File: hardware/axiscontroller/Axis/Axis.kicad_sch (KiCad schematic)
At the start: 62 parts, among them J1 RS485, J10 Fan, J2 Motor, J3 Limits, J4 RS485, J5 Console, J6 Temp A, J7 Temp B, J8 Brake, J9 Power, Q1 Q_NMOS, Q2 Q_NMOS, SW1 SW_DIP_x04, U4 TLP291, U5 TLP291, U6 TLP291, U7 MAX485CPA, U8 74AHCT125

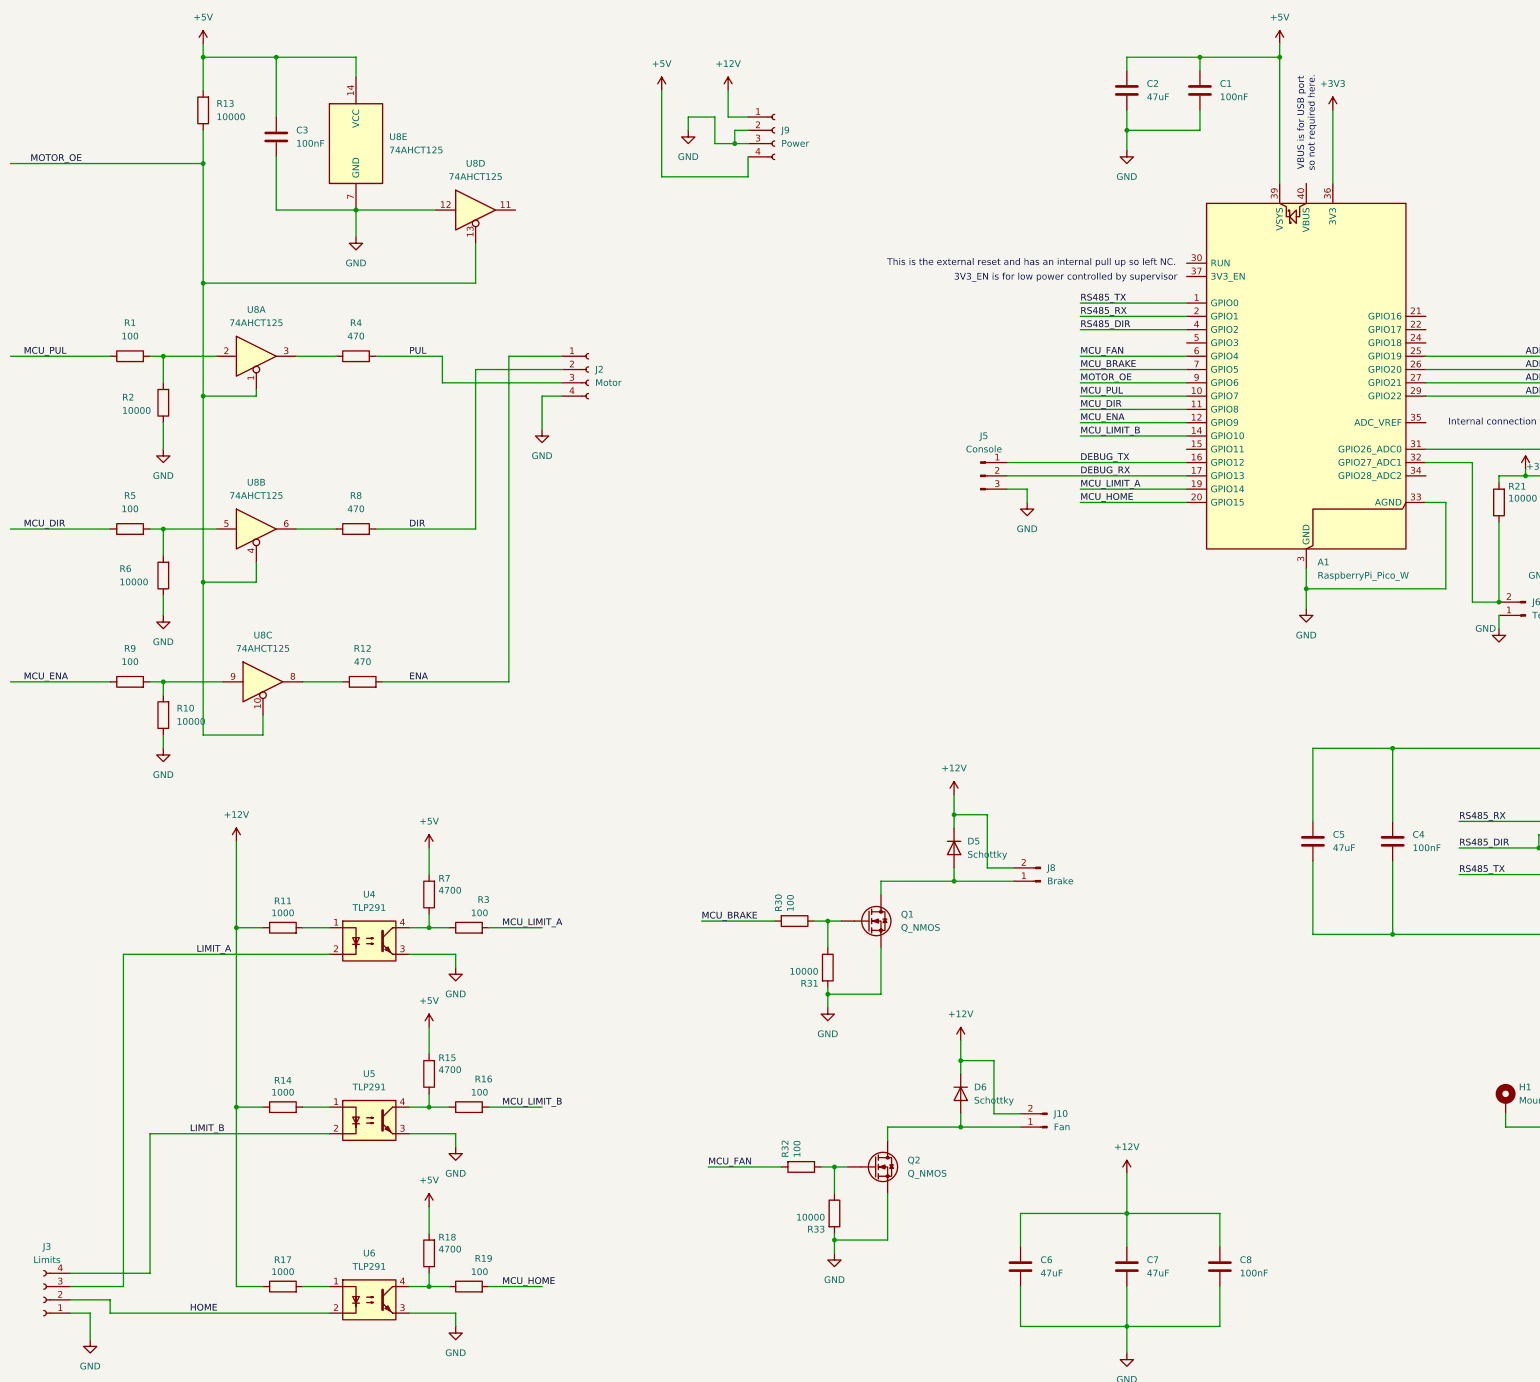
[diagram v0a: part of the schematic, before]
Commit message: Fix ERC warnings/errors and add IRLR8726 component.
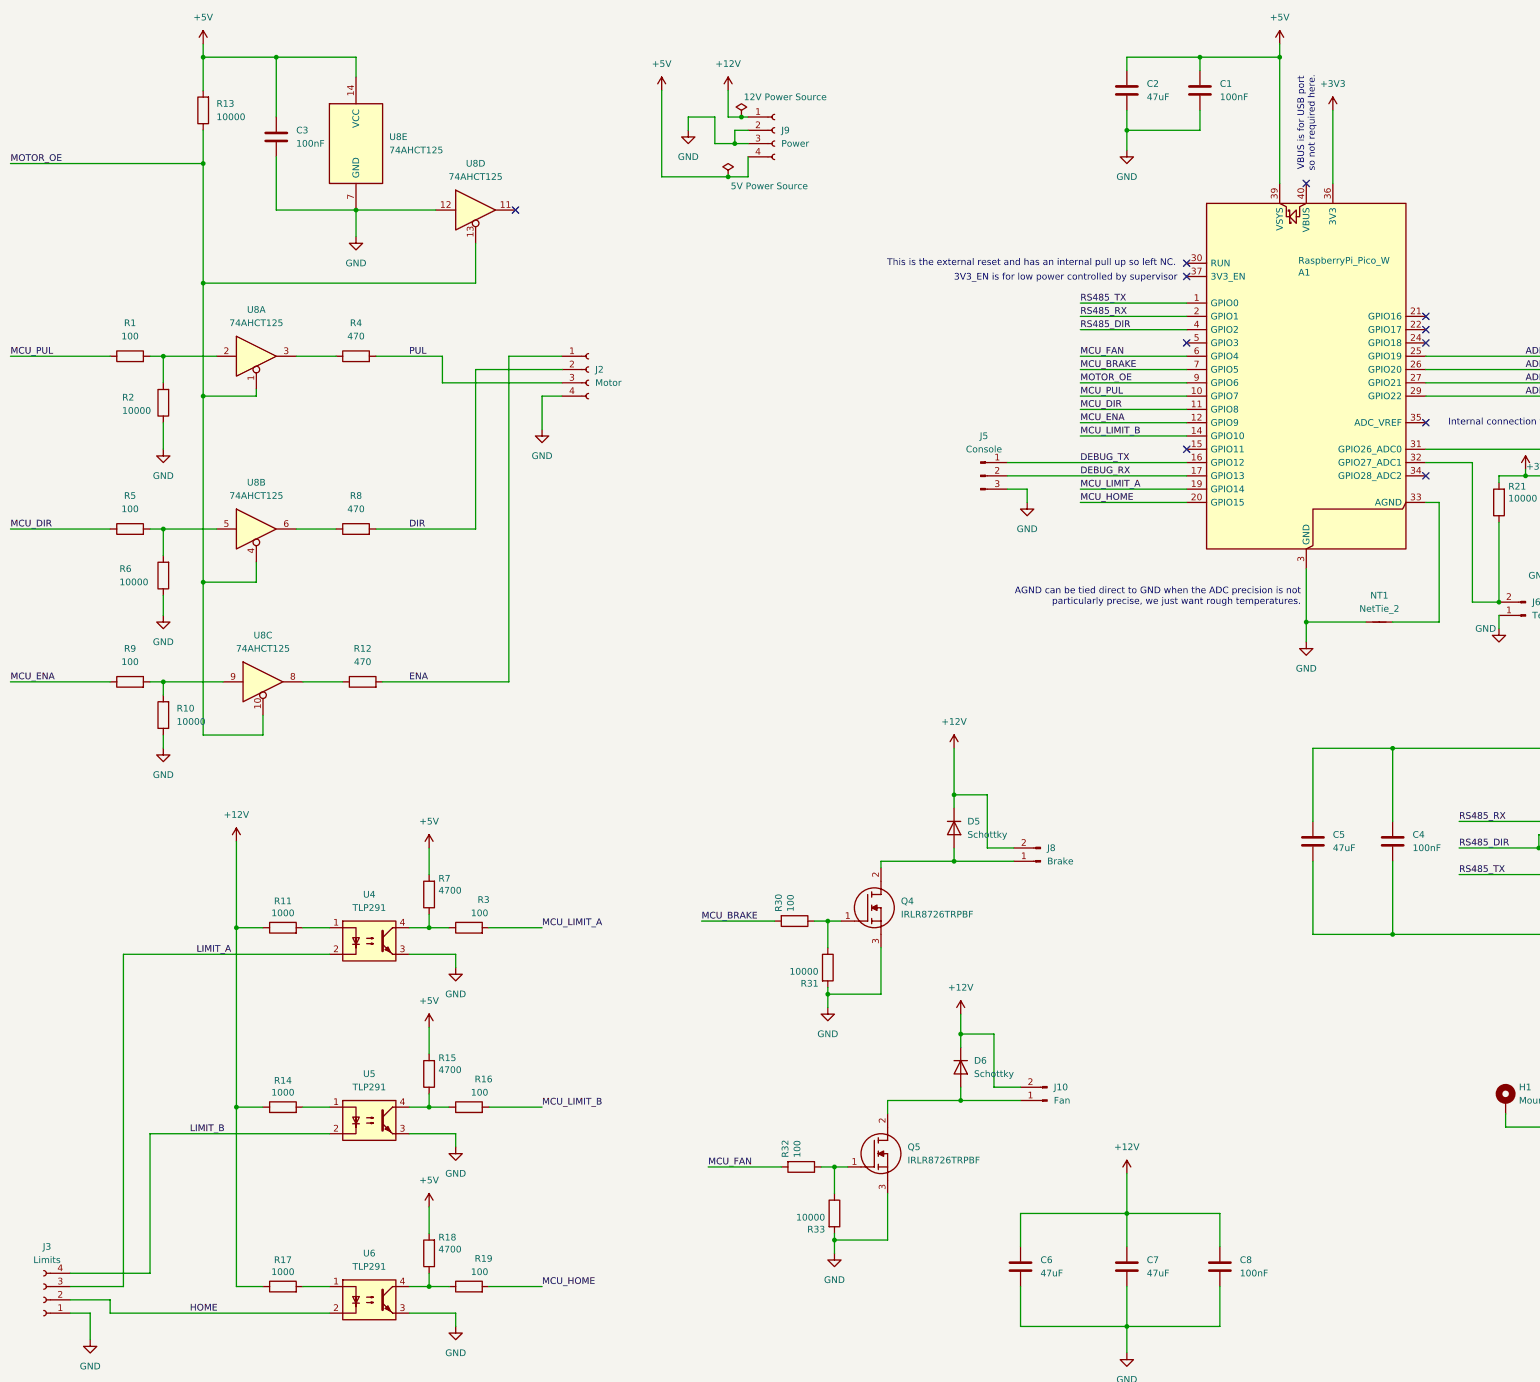
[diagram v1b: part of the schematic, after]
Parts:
- removed Q1, Q2: Q_NMOS, Package_TO_SOT_SMD:TO-252-2, symbol Device:Q_NMOS
- added NT1: NetTie_2, NetTie:NetTie-2_SMD_Pad2.0mm, symbol Device:NetTie_2
- added Q4, Q5: IRLR8726TRPBF, AJS_Roberta:IRLR8726TRPBF, symbol AJS_Roberta:IRLR8726TRPBF
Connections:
- net GND: now also NT1.1, Q4.3 (S), Q5.3 (S); no longer A1.33 (AGND)
- net at R30.1, R31.1: now also Q4.1 (G)
- net at D5.2 (A), J8.1 (Pin_1): now also Q4.2 (D)
- net at R32.1, R33.1: now also Q5.1 (G)
- net at D6.2 (A), J10.1 (Pin_1): now also Q5.2 (D)
- new net: A1.33 (AGND), NT1.2
- no-connect marks 0 -> 11
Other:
- note added: "AGND can be tied direct to GND when the ADC precision is not particularly precise, we just want rough temperatures."
- moved on the sheet: D5, D6, J10, J8

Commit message: The second revision of the robot axis controller.
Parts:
- removed A1: RaspberryPi_Pico_W, AJS_Roberta:PI_PICO2_SOCKET, symbol MCU_Module:RaspberryPi_Pico_W
- removed C1: 100nF, Capacitor_SMD:C_0805_2012Metric, symbol Device:C
- removed C2: 47uF, Capacitor_SMD:C_0805_2012Metric, symbol Device:C
- removed D2: SM712_SOT23, Package_TO_SOT_SMD:SOT-23, symbol Diode:SM712_SOT23
- removed D5, D6: Schottky, Diode_SMD:D_SMB-SMC_Universal_Handsoldering, symbol Device:D
- removed H1, H2, H3: MountingHole_Pad, MountingHole:MountingHole_2.2mm_M2_DIN965_Pad, symbol Mechanical:MountingHole_Pad
- removed J1, J4: RS485, AJS_Roberta:MOLEX_SL_70553_0002, symbol Connector:Conn_01x03_Socket
- removed J10: Fan, AJS_Roberta:MOLEX_SL_70553_0001, symbol Connector:Conn_01x02_Pin
- removed J2: Motor, AJS_Roberta:MOLEX_SL_70553_0003, symbol Connector:Conn_01x04_Socket
- removed J3: Limits, AJS_Roberta:MOLEX_SL_70553_0003, symbol Connector:Conn_01x04_Socket
- removed J5: Console, AJS_Roberta:MOLEX_SL_70553_0002, symbol Connector:Conn_01x03_Pin
- removed J6: Temp A, AJS_Roberta:MOLEX_SL_70553_0001, symbol Connector:Conn_01x02_Pin
- removed J7: Temp B, AJS_Roberta:MOLEX_SL_70553_0001, symbol Connector:Conn_01x02_Pin
- removed J8: Brake, AJS_Roberta:MOLEX_SL_70553_0001, symbol Connector:Conn_01x02_Pin
- removed J9: Power, AJS_Roberta:MOLEX-171857-0001, symbol Connector:Conn_01x04_Socket
- removed JP1: Termination, Connector_PinHeader_2.54mm:PinHeader_2x01_P2.54mm_Vertical, symbol Jumper:Jumper_2_Open
- removed NT1: NetTie_2, NetTie:NetTie-2_SMD_Pad2.0mm, symbol Device:NetTie_2
- removed Q4, Q5: IRLR8726TRPBF, AJS_Roberta:IRLR8726TRPBF, symbol AJS_Roberta:IRLR8726TRPBF
- removed R1, R16, R19, R3, R30, R32, R5, R9: 100, Resistor_SMD:R_0805_2012Metric_Pad1.20x1.40mm_HandSolder, symbol Device:R
- removed R10, R13, R2, R21, R29, R31, R33, R6: 10000, Resistor_SMD:R_0805_2012Metric_Pad1.20x1.40mm_HandSolder, symbol Device:R
- removed R11, R14, R17: 1000, Resistor_SMD:R_0805_2012Metric_Pad1.20x1.40mm_HandSolder, symbol Device:R
- removed R12, R4, R8: 470, Resistor_SMD:R_0805_2012Metric_Pad1.20x1.40mm_HandSolder, symbol Device:R
- removed R15, R18, R7: 4700, Resistor_SMD:R_0805_2012Metric_Pad1.20x1.40mm_HandSolder, symbol Device:R
- removed SW1: SW_DIP_x04, Package_DIP:DIP-8_W7.62mm, symbol Switch:SW_DIP_x04
- removed U4, U5, U6: TLP291, Package_SO:SOIC-4_4.55x2.6mm_P1.27mm, symbol Isolator:TLP291
- removed U8: 74AHCT125, Package_DIP:DIP-14_W7.62mm, symbol 74xx:74AHCT125
- added C10: 10uF, Capacitor_SMD:C_0805_2012Metric, symbol Device:C
- added C13: 47uF, Capacitor_SMD:C_0805_2012Metric, symbol Device:C
- added C16: 100nF, Capacitor_SMD:C_0805_2012Metric, symbol Device:C
- added D4, D5: CLMUD_FKC, AJS_Cree:CLMVC-FKC-CG1J1561BB7D3S3, symbol AJS_Cree:CLMUD_FKC
- added H1: MountingHole, MountingHole:MountingHole_6.5mm, symbol Mechanical:MountingHole
- added IC2: TCA6507PWR, AJS_TexasInstruments:TCA6507PWR, symbol AJS_TexasInstruments:TCA6507PWR
- added IC4: AT21CS01-STUM10-T, AJS_STMicro:AT21CS01-STUM10-T, symbol AJS_STMicro:AT21CS01-STUM10-T
- added J12: TC2050, Connector:Tag-Connect_TC2050-IDC-FP_2x05_P1.27mm_Vertical, symbol Connector:TC2050
- added J17, J19, J20, J21, J22: JST PH, Connector_JST:JST_PH_S2B-PH-K_1x02_P2.00mm_Horizontal, symbol Connector:Conn_01x02_Pin
- added J18: JST PH, Connector_JST:JST_PH_S8B-PH-K_1x08_P2.00mm_Horizontal, symbol Connector:Conn_01x08_Pin
- added J2: CL57_Driver, Connector_JST:JST_PH_S9B-PH-K_1x09_P2.00mm_Horizontal, symbol Connector:Conn_01x09_Pin
- added J3: ~, AJS_Molex:KK254-171857-0004, symbol Connector:Conn_01x04_Pin
- added J6: TE MicroMatch, AJS_TEConnectivity:MicroMatch_Locking_3380708, symbol Connector:Conn_01x08_Pin
- added J7: ~, Connector_PinHeader_2.54mm:PinHeader_1x08_P2.54mm_Vertical, symbol Connector:Conn_01x08_Pin
- added R19, R27, R52, R53, R55: 100, Resistor_SMD:R_0805_2012Metric, symbol AJS_Discretes:R_100
- added R26, R51: 100K, Resistor_SMD:R_0805_2012Metric, symbol AJS_Discretes:R_100K
- added R29, R35: 10000, Resistor_SMD:R_0805_2012Metric, symbol AJS_Discretes:R_10K
- added R54, R60, R61, R62, R63, R64: 330, Resistor_SMD:R_0805_2012Metric, symbol AJS_Discretes:R_330
- added SW1: SW_Tactile_6mm, AJS_SameSky:Tactile_6mm_6mm_4.5mm, symbol AJS_Discretes:SW_Tactile_6mm
- added U2: AMS1117-3.3, Package_TO_SOT_SMD:SOT-223-3_TabPin2, symbol Regulator_Linear:AMS1117-3.3
- C3: value 100nF -> 10uF; CPC CA06466 -> CA10304; Part MC0805B104K500CT -> GRT21BR60J476ME13L
- R20, R22: footprint Resistor_SMD:R_0805_2012Metric_Pad1.20x1.40mm_HandSolder -> Resistor_SMD:R_0805_2012Metric; symbol Device:R -> AJS_Discretes:R_47; Mouser (none) -> 71-CRCW0805-47-E3
- R23: footprint Resistor_SMD:R_0805_2012Metric_Pad1.20x1.40mm_HandSolder -> Resistor_SMD:R_0805_2012Metric; symbol Device:R -> AJS_Discretes:R_120; Mouser (none) -> 71-CRCW0805120RFKEA; now not fitted
- U7: footprint Package_DIP:DIP-8_W7.62mm -> Package_SO:SOIC-8_3.9x4.9mm_P1.27mm
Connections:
- net +12V: now also J17.1 (Pin_1), J18.1 (Pin_1), J18.3 (Pin_3), J18.5 (Pin_5), J18.7 (Pin_7), J19.1 (Pin_1), J20.1 (Pin_1), J3.4 (Pin_4)
- net +3V3: now also C4.1, C5.1, U7.8 (VCC), C10.1, C13.1, C16.1, D4.1 (A), D5.1 (A), IC2.1 (VCC), J12.1, R26.1, R29.2, R35.2, R51.1, U2.2 (VO)
- net +5V: now also J3.1 (Pin_1), U2.3 (VI); no longer C4.1, C5.1, U7.8 (VCC)
- net GND: now also C10.2, C13.2, C16.2, IC2.5 (GND), IC4.3 (GND), J12.3, J12.5, J2.9 (Pin_9), J21.1 (Pin_1), J22.1 (Pin_1), J3.2 (Pin_2), J3.3 (Pin_3), J6.1 (Pin_1), J6.8 (Pin_8), J7.1 (Pin_1), J7.8 (Pin_8), SW1.1, U2.1 (GND)
- net RS485_B: now reaches R22.1, R23.2
- net RS485_B: now also J6.4 (Pin_4), J7.4 (Pin_4)
- net RS485_A: now reaches R20.1
- net RS485_A: now also R23.1, J6.3 (Pin_3), J7.3 (Pin_3)
- net RS485_DIR renamed MicroController/RS485_DIR
- net RS485_RX renamed MicroController/RS485_RX
- net RS485_TX renamed MicroController/RS485_TX
- new net: IC2.13 (P5), R61.1
- new net: D4.4 (BK), R61.2
- new net: IC2.8 (P0), R64.1
- new net: D5.4 (BK), R64.2
- new net: D5.2 (RK), R62.2
- new net: D5.3 (GK), R63.2
- new net: J6.6 (Pin_6), J7.6 (Pin_6)
- new net: D4.2 (RK), R54.2
- new net: D4.3 (GK), R60.2
- new net: IC2.12 (P4), R60.1
- new net: IC2.10 (P2), R62.1
- new net: IC2.11 (P3), R54.1
- new net: IC2.9 (P1), R63.1
- new net ALARM: J2.7 (Pin_7), R51.2, R52.2
- new net BOOT: J6.2 (Pin_2), J7.2 (Pin_2), R27.1
- new net DIR+: J2.3 (Pin_3)
- new net DIR-: J2.4 (Pin_4)
- new net ENA+: J2.5 (Pin_5)
- new net ENA-: J2.6 (Pin_6)
- new net ESTOP: J6.7 (Pin_7), J7.7 (Pin_7), R19.1
- new net INPOS: J2.8 (Pin_8), R26.2, R53.2
- new net MicroController/BOOT: R27.2
- new net MicroController/ESTOP: R19.2
- new net MicroController/LED_OE: IC2.4 (EN)
- new net MicroController/MOTOR_ALARM: R52.1
- new net MicroController/MOTOR_INPOS: R53.1
- new net MicroController/NRST: SW1.2
- new net MicroController/SCL: IC2.2 (SCL)
- new net MicroController/SDA: IC2.3 (SDA)
- new net MicroController/SIO: IC4.1 (SI/O)
- new net MicroController/SWDCLK/BOOT: J12.4
- new net MicroController/SWDIO: J12.2
- new net MicroController/SWDRST: J12.10
- new net MicroController/SYNC: R55.2
- new net MicroController/TEMP_A: J21.2 (Pin_2), R35.1
- new net MicroController/TEMP_B: J22.2 (Pin_2), R29.1
- new net Opto Input 1/SWITCH-: J18.2 (Pin_2)
- new net Opto Input 2/SWITCH-: J18.4 (Pin_4)
- new net Opto Input 3/SWITCH-: J18.6 (Pin_6)
- new net Opto Input 4/SWITCH-: J18.8 (Pin_8)
- new net PUL+: J2.1 (Pin_1)
- new net PUL-: J2.2 (Pin_2)
- new net Power Output A/Load-: J19.2 (Pin_2)
- new net Power Output B/Load-: J17.2 (Pin_2)
- new net Power Output C/Load-: J20.2 (Pin_2)
- new net SYNC: J6.5 (Pin_5), J7.5 (Pin_5), R55.1
- no-connect marks 11 -> 7
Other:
- added sheet Line Driver 1 (linedriver.kicad_sch)
- added sheet Line Driver 2 (linedriver.kicad_sch)
- added sheet Line Driver 3 (linedriver.kicad_sch)
- added sheet Master (master.kicad_sch)
- added sheet MicroController (mcu.kicad_sch)
- added sheet Opto Input 1 (optoinput.kicad_sch)
- added sheet Opto Input 2 (optoinput.kicad_sch)
- added sheet Opto Input 3 (optoinput.kicad_sch)
- added sheet Opto Input 4 (optoinput.kicad_sch)
- added sheet Power Output A (poweroutputs.kicad_sch)
- added sheet Power Output B (poweroutputs.kicad_sch)
- added sheet Power Output C (poweroutputs.kicad_sch)
- note added: "Broken out into individual two pin JST PHs as each one is likely going somewhere completely different and a loom would be overkill here."
- note added: "Single ended signals fine within a PCB cluster and the master will provide the pull down and any RC debouncing if required,"
- note added: "TE Micro Match Modern 1.27mm IDC Header Additional Debug header"
- note added: "The ALARM and BRK (in position) signals are opto outputs in the CL57T so we pull them high and it switches them to ground when active."
- note added: "These are bulk decoupling for the 12V domain."
- note added: "These are laid out in the same order as the CL57T so the wiring is neat. But I still can't bring myself to use screw termninals so these are crimped JST PHs."
- note added: "This one is OK to use a single 8 way connector as it will be connected to the four pairs of a Cat5 cable all going off to the axis joint."
- note removed: "3V3_EN is for low power controlled by supervisor"
- note removed: "AGND can be tied direct to GND when the ADC precision is not particularly precise, we just want rough temperatures."
- note removed: "Internal connection to 3V3"
- note removed: "This is the external reset and has an internal pull up so left NC."
- note removed: "VBUS is for USB port so not required here."
- moved on the sheet: C4, C5, C6, C7, C8, R20, R22, U7
